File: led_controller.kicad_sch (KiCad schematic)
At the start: 55 parts, among them J1 Screw_Terminal_01x02, J10 Conn_01x03, J2 SJ-3524-SMT, J3 Conn_01x03, J4 Conn_01x03, J5 Conn_01x03, J6 Conn_01x03, J7 Conn_01x03, J8 Conn_01x03, J9 Conn_01x03, SW1 RotaryEncoder_Switch, U1 MAX9814, U2 74HCT245, U3 Teensy4.0, U4 Adafruit_TFT_1in3_ST7789

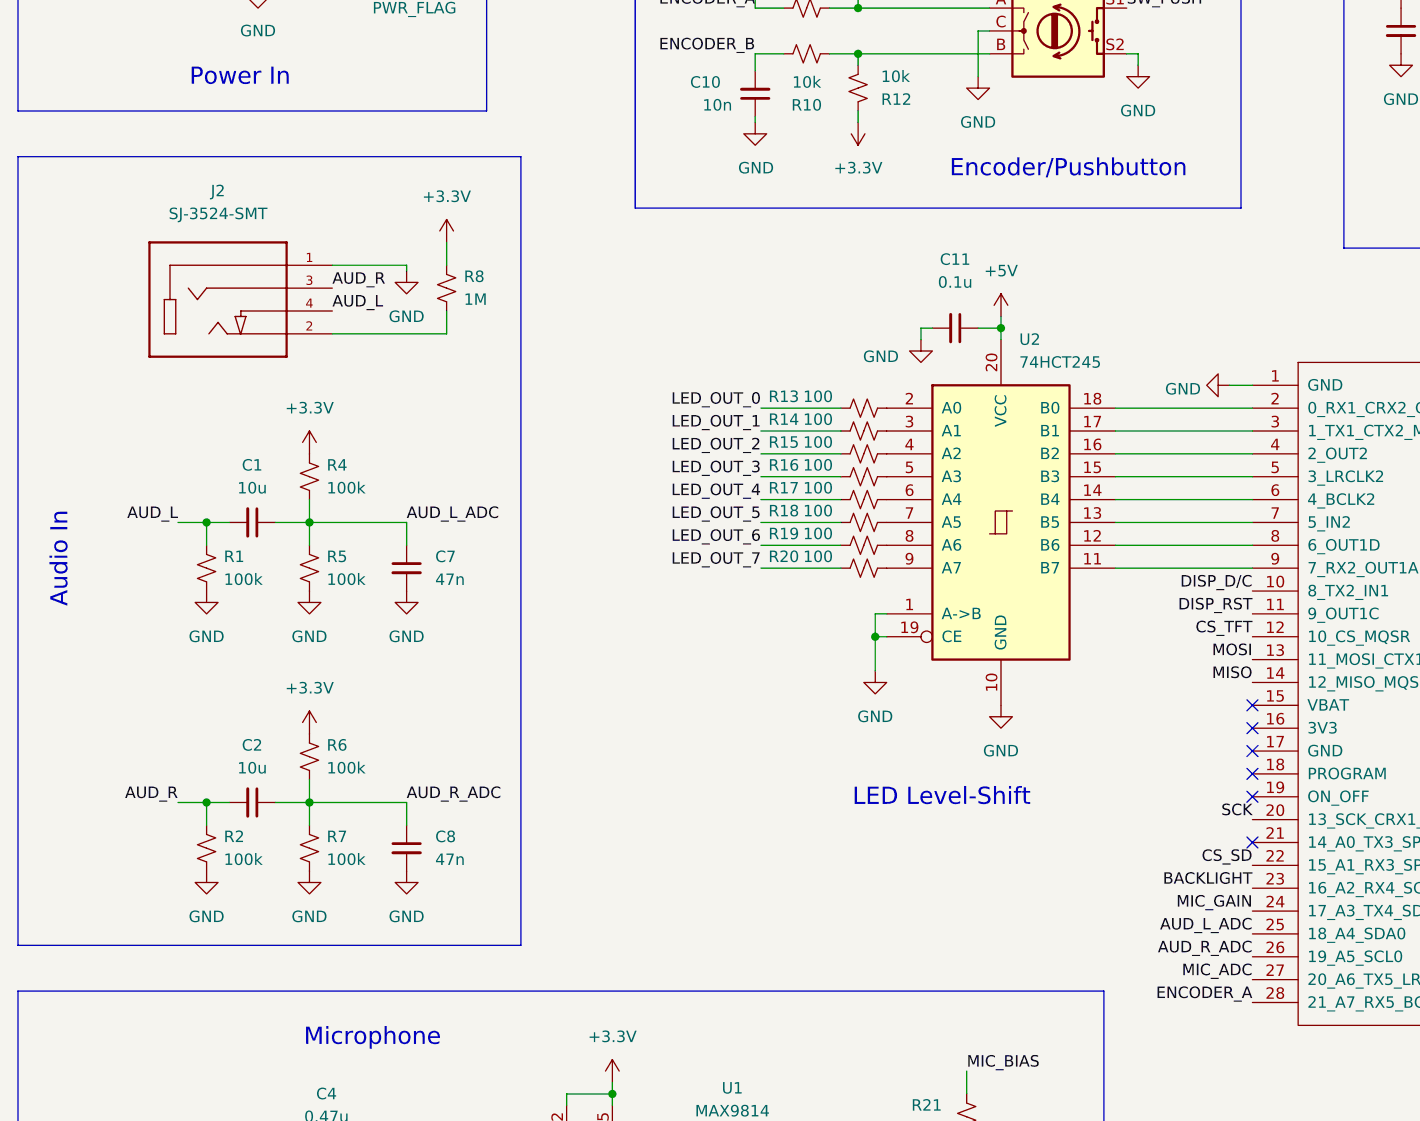
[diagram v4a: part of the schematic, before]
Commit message: Fix audio jack pinout and route jack insertion pin
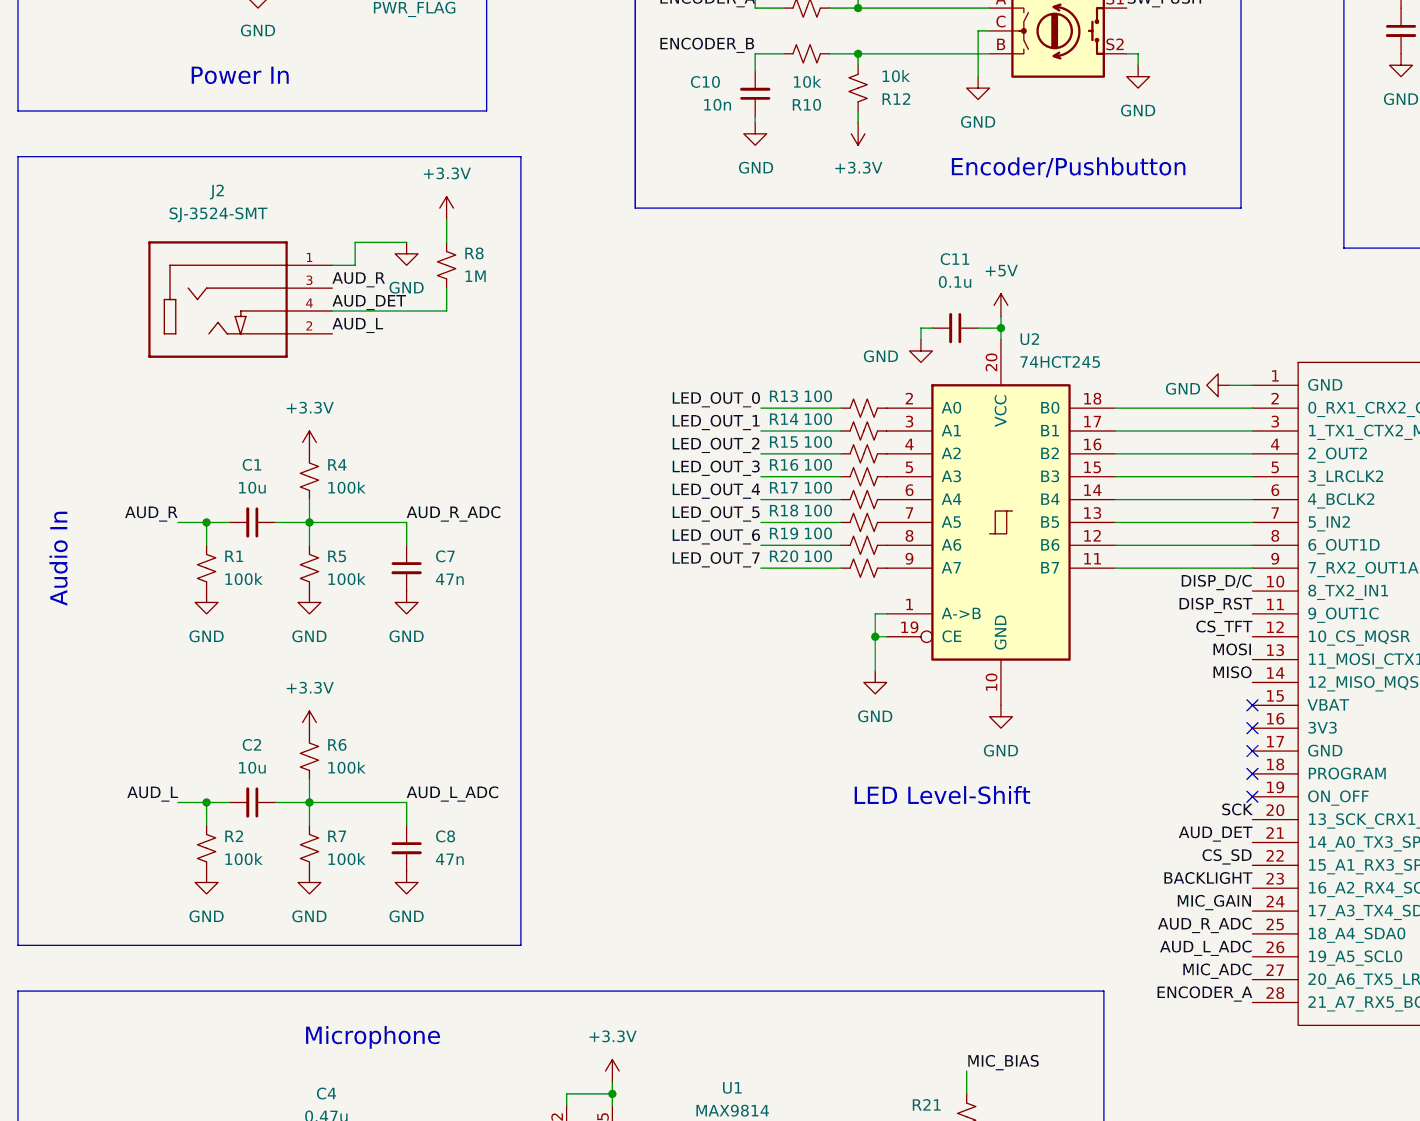
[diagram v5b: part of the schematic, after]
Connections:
- net AUD_L: now also C2.2, J2.2, R2.1; no longer C1.2, J2.4, R1.1
- net AUD_L_ADC: now also C2.1, C8.1, R6.2, R7.1, U3.26 (19_A5_SCL0); no longer C1.1, C7.1, R4.2, R5.1, U3.25 (18_A4_SDA0)
- net AUD_R: now also C1.2, R1.1; no longer C2.2, R2.1
- net AUD_R_ADC: now also C1.1, C7.1, R4.2, R5.1, U3.25 (18_A4_SDA0); no longer C2.1, C8.1, R6.2, R7.1, U3.26 (19_A5_SCL0)
- net AUD_DET: now reaches R8.2
- net AUD_DET: now also J2.4, U3.21 (14_A0_TX3_SPDIF_OUT); no longer J2.2
- no-connect marks 28 -> 27
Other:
- moved on the sheet: R8
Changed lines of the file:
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@@
   (no_connect (at 209.55 96.52))
   (no_connect (at 209.55 86.36))
-  (no_connect (at 153.67 124.46))
   (no_connect (at 209.55 119.38))
   (no_connect (at 209.55 114.3))
@@
     (stroke (width 0) (type default) (color 0 0 0 0))
   )
-  (wire (pts (xy 64.135 57.785) (xy 64.135 60.325))
+  (wire (pts (xy 64.135 55.245) (xy 64.135 57.785))
     (stroke (width 0) (type default) (color 0 0 0 0))
   )
@@
     (stroke (width 0) (type default) (color 0 0 0 0))
   )
+  (wire (pts (xy 53.975 60.325) (xy 53.975 57.785))
+    (stroke (width 0) (type default) (color 0 0 0 0))
+  )
   (wire (pts (xy 125.73 66.04) (xy 125.73 67.31))
     (stroke (width 0) (type default) (color 0 0 0 0))
@@
     (stroke (width 0) (type default) (color 0 0 0 0))
   )
-  (wire (pts (xy 64.135 67.945) (xy 64.135 65.405))
+  (wire (pts (xy 64.135 65.405) (xy 64.135 62.865))
     (stroke (width 0) (type default) (color 0 0 0 0))
   )
@@
     (stroke (width 0) (type default) (color 0 0 0 0))
   )
-  (wire (pts (xy 51.435 67.945) (xy 64.135 67.945))
+  (wire (pts (xy 51.435 65.405) (xy 64.135 65.405))
     (stroke (width 0) (type default) (color 0 0 0 0))
   )
@@
     (stroke (width 0) (type default) (color 0 0 0 0))
   )
+  (wire (pts (xy 53.975 57.785) (xy 59.69 57.785))
+    (stroke (width 0) (type default) (color 0 0 0 0))
+  )
   (wire (pts (xy 39.37 168.91) (xy 36.83 168.91))
     (stroke (width 0) (type default) (color 0 0 0 0))
@@
     (stroke (width 0) (type default) (color 0 0 0 0))
   )
-  (wire (pts (xy 51.435 60.325) (xy 59.69 60.325))
-    (stroke (width 0) (type default) (color 0 0 0 0))
-  )
   (wire (pts (xy 138.43 93.98) (xy 153.67 93.98))
     (stroke (width 0) (type default) (color 0 0 0 0))
@@
     (stroke (width 0) (type default) (color 0 0 0 0))
   )
-  (wire (pts (xy 59.69 60.325) (xy 59.69 60.96))
-    (stroke (width 0) (type default) (color 0 0 0 0))
-  )
   (polyline (pts (xy 72.39 135.89) (xy 16.51 135.89))
     (stroke (width 0) (type default) (color 0 0 0 0))
@@
   )
   (polyline (pts (xy 237.49 151.13) (xy 237.49 52.07))
+    (stroke (width 0) (type default) (color 0 0 0 0))
+  )
+  (wire (pts (xy 51.435 60.325) (xy 53.975 60.325))
     (stroke (width 0) (type default) (color 0 0 0 0))
   )
@@
     (effects (font (size 1.905 1.905)) (justify left bottom))
   )
-  (label "AUD_L_ADC" (at 153.67 134.62 180)
+  (label "AUD_R_ADC" (at 153.67 134.62 180)
     (effects (font (size 1.27 1.27)) (justify right bottom))
   )
@@
   (label "DISP_RST" (at 153.67 99.06 180)
     (effects (font (size 1.27 1.27)) (justify right bottom))
+  )
+  (label "AUD_DET" (at 51.435 65.405 0)
+    (effects (font (size 1.27 1.27)) (justify left bottom))
   )
   (label "BACKLIGHT" (at 189.23 49.53 0)
@@
     (effects (font (size 1.27 1.27)) (justify right bottom))
   )
+  (label "AUD_DET" (at 153.67 124.46 180)
+    (effects (font (size 1.27 1.27)) (justify right bottom))
+  )
   (label "MIC_ADC" (at 105.41 171.45 0)
     (effects (font (size 1.27 1.27)) (justify left bottom))
@@
     (effects (font (size 1.27 1.27)) (justify right bottom))
   )
-  (label "AUD_R_ADC" (at 153.67 137.16 180)
+  (label "AUD_L_ADC" (at 153.67 137.16 180)
     (effects (font (size 1.27 1.27)) (justify right bottom))
   )
@@
     (effects (font (size 1.27 1.27)) (justify right bottom))
   )
-  (label "AUD_L" (at 51.435 65.405 0)
-    (effects (font (size 1.27 1.27)) (justify left bottom))
-  )
   (label "LED_OUT_6" (at 259.715 127 180)
     (effects (font (size 1.27 1.27)) (justify right bottom))
@@
     (effects (font (size 1.27 1.27)) (justify left bottom))
   )
+  (label "AUD_L" (at 51.435 67.945 0)
+    (effects (font (size 1.27 1.27)) (justify left bottom))
+  )
   (label "MIC_ADC" (at 153.67 139.7 180)
     (effects (font (size 1.27 1.27)) (justify right bottom))
@@
     (effects (font (size 1.27 1.27)) (justify right bottom))
   )
-  (label "AUD_R" (at 34.29 120.015 180)
+  (label "AUD_L" (at 34.29 120.015 180)
     (effects (font (size 1.27 1.27)) (justify right bottom))
   )
@@
     (effects (font (size 1.27 1.27)) (justify right bottom))
   )
-  (label "AUD_L_ADC" (at 59.69 88.9 0)
+  (label "AUD_R_ADC" (at 59.69 88.9 0)
     (effects (font (size 1.27 1.27)) (justify left bottom))
   )
@@
     (effects (font (size 1.27 1.27)) (justify left bottom))
   )
-  (label "AUD_R_ADC" (at 59.69 120.015 0)
+  (label "AUD_L_ADC" (at 59.69 120.015 0)
     (effects (font (size 1.27 1.27)) (justify left bottom))
   )
-  (label "AUD_L" (at 34.29 88.9 180)
+  (label "AUD_R" (at 34.29 88.9 180)
     (effects (font (size 1.27 1.27)) (justify right bottom))
   )
@@
     (pin "1")
   )
-  (symbol (lib_id "Device:R_Small_US") (at 64.135 62.865 0) (unit 1)
-    (in_bom yes) (on_board yes) (fields_autoplaced)
-    (property "Reference" "R8" (id 0) (at 66.04 61.5949 0)
-      (effects (font (size 1.27 1.27)) (justify left))
-    )
-    (property "Value" "1M" (id 1) (at 66.04 64.1349 0)
-      (effects (font (size 1.27 1.27)) (justify left))
-    )
-    (property "Footprint" "Resistor_SMD:R_0805_2012Metric_Pad1.20x1.40mm_HandSolder" (id 2) (at 64.135 62.865 0)
-      (effects (font (size 1.27 1.27)) hide)
-    )
-    (property "Datasheet" "~" (id 3) (at 64.135 62.865 0)
+  (symbol (lib_id "Device:R_Small_US") (at 64.135 60.325 0) (unit 1)
+    (in_bom yes) (on_board yes) (fields_autoplaced)
+    (property "Reference" "R8" (id 0) (at 66.04 59.0549 0)
+      (effects (font (size 1.27 1.27)) (justify left))
+    )
+    (property "Value" "1M" (id 1) (at 66.04 61.5949 0)
+      (effects (font (size 1.27 1.27)) (justify left))
+    )
+    (property "Footprint" "Resistor_SMD:R_0805_2012Metric_Pad1.20x1.40mm_HandSolder" (id 2) (at 64.135 60.325 0)
+      (effects (font (size 1.27 1.27)) hide)
+    )
+    (property "Datasheet" "~" (id 3) (at 64.135 60.325 0)
       (effects (font (size 1.27 1.27)) hide)
     )
@@
     (pin "2")
   )
-  (symbol (lib_id "power:GND") (at 59.69 60.96 0) (unit 1)
-    (in_bom yes) (on_board yes) (fields_autoplaced)
-    (property "Reference" "#PWR013" (id 0) (at 59.69 67.31 0)
-      (effects (font (size 1.27 1.27)) hide)
-    )
-    (property "Value" "GND" (id 1) (at 59.69 66.04 0))
-    (property "Footprint" "" (id 2) (at 59.69 60.96 0)
-      (effects (font (size 1.27 1.27)) hide)
-    )
-    (property "Datasheet" "" (id 3) (at 59.69 60.96 0)
+  (symbol (lib_id "power:GND") (at 59.69 57.785 0) (unit 1)
+    (in_bom yes) (on_board yes) (fields_autoplaced)
+    (property "Reference" "#PWR013" (id 0) (at 59.69 64.135 0)
+      (effects (font (size 1.27 1.27)) hide)
+    )
+    (property "Value" "GND" (id 1) (at 59.69 62.865 0))
+    (property "Footprint" "" (id 2) (at 59.69 57.785 0)
+      (effects (font (size 1.27 1.27)) hide)
+    )
+    (property "Datasheet" "" (id 3) (at 59.69 57.785 0)
       (effects (font (size 1.27 1.27)) hide)
     )
@@
     (pin "1")
   )
-  (symbol (lib_id "power:+3.3V") (at 64.135 57.785 0) (unit 1)
-    (in_bom yes) (on_board yes) (fields_autoplaced)
-    (property "Reference" "#PWR017" (id 0) (at 64.135 61.595 0)
-      (effects (font (size 1.27 1.27)) hide)
-    )
-    (property "Value" "+3.3V" (id 1) (at 64.135 52.705 0))
-    (property "Footprint" "" (id 2) (at 64.135 57.785 0)
-      (effects (font (size 1.27 1.27)) hide)
-    )
-    (property "Datasheet" "" (id 3) (at 64.135 57.785 0)
-      (effects (font (size 1.27 1.27)) hide)
-    )
+  (symbol (lib_id "power:+3.3V") (at 64.135 55.245 0) (unit 1)
+    (in_bom yes) (on_board yes) (fields_autoplaced)
+    (property "Reference" "#PWR017" (id 0) (at 64.135 59.055 0)
+      (effects (font (size 1.27 1.27)) hide)
+    )
+    (property "Value" "+3.3V" (id 1) (at 64.135 50.165 0))
+    (property "Footprint" "" (id 2) (at 64.135 55.245 0)
+      (effects (font (size 1.27 1.27)) hide)
+    )
+    (property "Datasheet" "" (id 3) (at 64.135 55.245 0)
+      (effects (font (size 1.27 1.27)) hide)
+    )

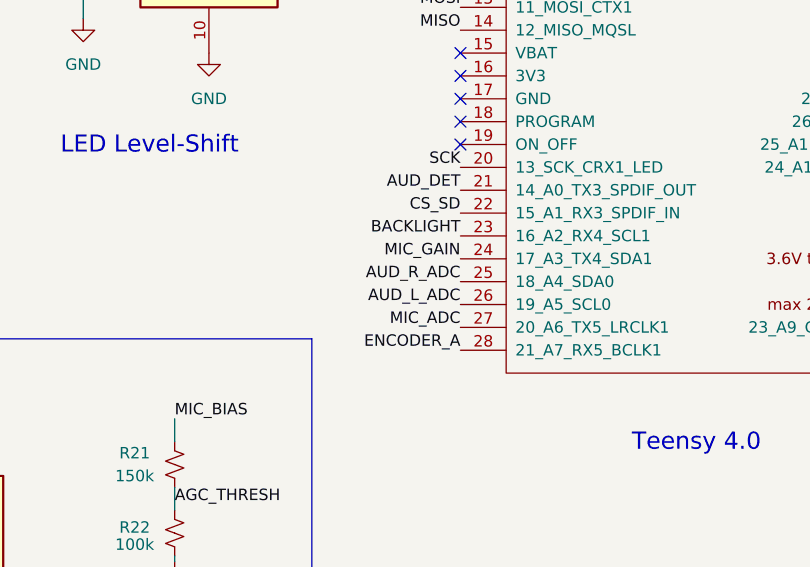
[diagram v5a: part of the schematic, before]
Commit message: Rearrange some analog pins, tweak routing
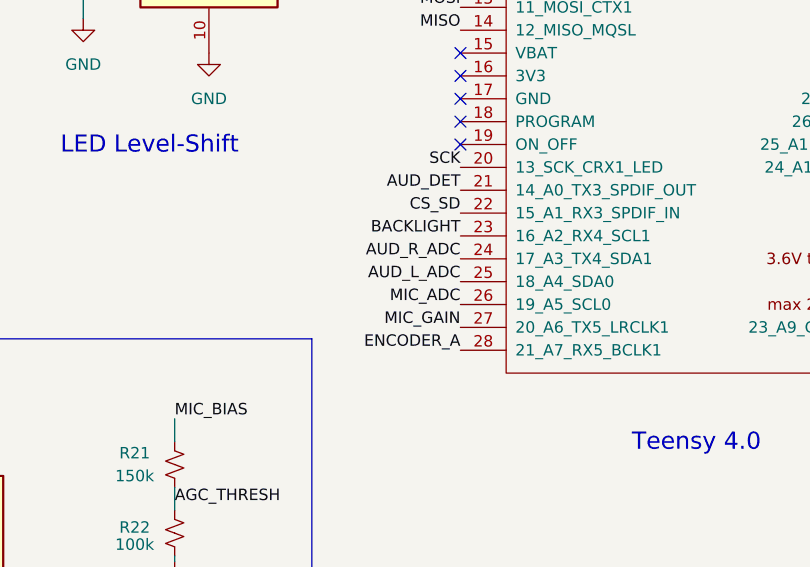
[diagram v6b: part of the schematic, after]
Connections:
- net AUD_L_ADC: now also U3.25 (18_A4_SDA0); no longer U3.26 (19_A5_SCL0)
- net AUD_R_ADC: now also U3.24 (17_A3_TX4_SDA1); no longer U3.25 (18_A4_SDA0)
- net MIC_ADC: now also U3.26 (19_A5_SCL0); no longer U3.27 (20_A6_TX5_LRCLK1)
- net MIC_GAIN: now also U3.27 (20_A6_TX5_LRCLK1); no longer U3.24 (17_A3_TX4_SDA1)
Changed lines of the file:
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@@
     (effects (font (size 1.905 1.905)) (justify left bottom))
   )
-  (label "AUD_R_ADC" (at 153.67 134.62 180)
+  (label "AUD_R_ADC" (at 153.67 132.08 180)
     (effects (font (size 1.27 1.27)) (justify right bottom))
   )
@@
     (effects (font (size 1.27 1.27)) (justify right bottom))
   )
-  (label "MIC_GAIN" (at 153.67 132.08 180)
+  (label "MIC_GAIN" (at 153.67 139.7 180)
     (effects (font (size 1.27 1.27)) (justify right bottom))
   )
@@
     (effects (font (size 1.27 1.27)) (justify right bottom))
   )
-  (label "AUD_L_ADC" (at 153.67 137.16 180)
+  (label "AUD_L_ADC" (at 153.67 134.62 180)
     (effects (font (size 1.27 1.27)) (justify right bottom))
   )
@@
     (effects (font (size 1.27 1.27)) (justify left bottom))
   )
-  (label "MIC_ADC" (at 153.67 139.7 180)
+  (label "MIC_ADC" (at 153.67 137.16 180)
     (effects (font (size 1.27 1.27)) (justify right bottom))
   )

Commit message: some more tweaks
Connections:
- net AUD_L_ADC: now also U3.23 (16_A2_RX4_SCL1); no longer U3.25 (18_A4_SDA0)
- net AUD_R_ADC: now also U3.22 (15_A1_RX3_SPDIF_IN); no longer U3.24 (17_A3_TX4_SDA1)
- net BACKLIGHT: now also U3.25 (18_A4_SDA0); no longer U3.23 (16_A2_RX4_SCL1)
- net CS_SD: now also U3.24 (17_A3_TX4_SDA1); no longer U3.22 (15_A1_RX3_SPDIF_IN)
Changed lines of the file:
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@@
     (effects (font (size 1.905 1.905)) (justify left bottom))
   )
-  (label "AUD_R_ADC" (at 153.67 132.08 180)
+  (label "AUD_R_ADC" (at 153.67 127 180)
     (effects (font (size 1.27 1.27)) (justify right bottom))
   )
-  (label "BACKLIGHT" (at 153.67 129.54 180)
+  (label "BACKLIGHT" (at 153.67 134.62 180)
     (effects (font (size 1.27 1.27)) (justify right bottom))
   )
@@
     (effects (font (size 1.27 1.27)) (justify right bottom))
   )
-  (label "AUD_L_ADC" (at 153.67 134.62 180)
+  (label "AUD_L_ADC" (at 153.67 129.54 180)
     (effects (font (size 1.27 1.27)) (justify right bottom))
   )
@@
     (effects (font (size 1.27 1.27)) (justify left bottom))
   )
-  (label "CS_SD" (at 153.67 127 180)
+  (label "CS_SD" (at 153.67 132.08 180)
     (effects (font (size 1.27 1.27)) (justify right bottom))
   )
